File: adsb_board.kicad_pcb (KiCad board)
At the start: 2 copper layers, 50 x 25 mm, 13 parts, among them J1 Conn_Coaxial, J2 Conn_Coaxial, J3 USB_B_Micro, U1 TA1090EC, U2 TA1090EC, U3 PSA4-5043+

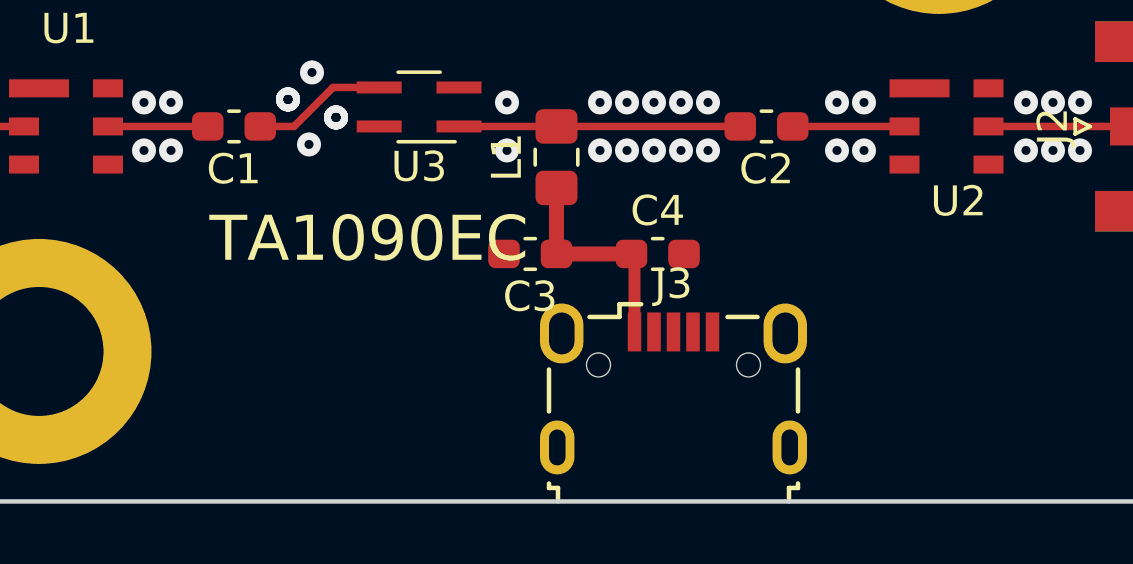
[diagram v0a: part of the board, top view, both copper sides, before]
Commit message: add ferrite bead in supply line
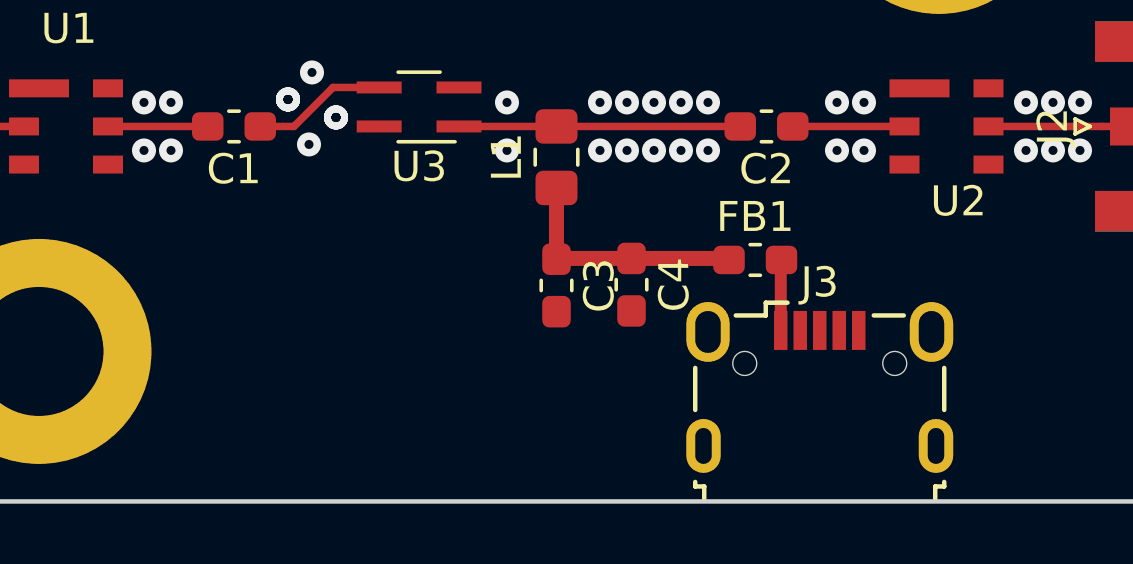
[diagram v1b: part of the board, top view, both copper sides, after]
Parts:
- added FB1: Ferrite_Bead, Resistor_SMD:R_0603_1608Metric_Pad1.05x0.95mm_HandSolder, F.Cu at (133.9, 92.0)
- moved J3 4.88 mm to (136.0, 96.2)
- moved C3 1.37 mm to (127.2, 92.8), turned to 270 degrees
- moved C4 1.35 mm to (129.8, 92.8), turned to 270 degrees
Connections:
- J3 pad 1: /VCC -> Net-(FB1-Pad2)
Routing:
- net Net-(FB1-Pad2): track 0.00 -> 2.36 mm
- net /VCC: track 7.34 -> 8.16 mm
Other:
- board text removed: "TA1090EC"
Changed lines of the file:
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@@
   (general
     (thickness 1.6)
-    (drawings 8)
-    (tracks 57)
+    (drawings 7)
+    (tracks 60)
     (zones 0)
-    (modules 13)
-    (nets 13)
+    (modules 14)
+    (nets 14)
   )
   (page A4)
@@
     (35 F.Paste user hide)
     (36 B.SilkS user hide)
-    (37 F.SilkS user hide)
+    (37 F.SilkS user)
     (38 B.Mask user hide)
     (39 F.Mask user hide)
-    (40 Dwgs.User user)
+    (40 Dwgs.User user hide)
     (41 Cmts.User user)
-    (42 Eco1.User user)
+    (42 Eco1.User user hide)
     (43 Eco2.User user)
     (44 Edge.Cuts user)
     (45 Margin user)
     (46 B.CrtYd user)
-    (47 F.CrtYd user)
+    (47 F.CrtYd user hide)
     (48 B.Fab user)
-    (49 F.Fab user)
+    (49 F.Fab user hide)
   )
   (setup
-    (last_trace_width 0.25)
+    (last_trace_width 0.5)
     (user_trace_width 0.3)
     (user_trace_width 0.4)
@@
   (net 11 "Net-(J3-Pad3)")
   (net 12 "Net-(J3-Pad4)")
+  (net 13 "Net-(FB1-Pad2)")
   (net_class Default "Dies ist die voreingestellte Netzklasse."
     (clearance 0.2)
@@
     (add_net "Net-(C2-Pad1)")
     (add_net "Net-(C2-Pad2)")
+    (add_net "Net-(FB1-Pad2)")
     (add_net "Net-(J3-Pad2)")
     (add_net "Net-(J3-Pad3)")
@@
     (add_net "Net-(U3-Pad4)")
   )
+  (module Resistor_SMD:R_0603_1608Metric_Pad1.05x0.95mm_HandSolder (layer F.Cu)
+    (at 133.875 91.95)
+    (descr "Resistor SMD 0603 (1608 Metric), square (rectangular) end terminal, IPC_7351 nominal with elongated pad for handsoldering. (Body size source: http://www.tortai-tech.com/upload/download/2011102023233369053.pdf), generated with kicad-footprint-generator")
+    (tags "resistor handsolder")
+    (attr smd)
+    (fp_text reference FB1 (at 0 -1.43) (layer F.SilkS)
+      (effects (font (size 1 1) (thickness 0.15)))
+    )
+    (fp_text value Ferrite_Bead (at 6.375 0.05) (layer F.Fab)
+      (effects (font (size 1 1) (thickness 0.15)))
+    )
+    (fp_line (start -0.8 0.4) (end -0.8 -0.4) (layer F.Fab) (width 0.1))
+    (fp_line (start -0.8 -0.4) (end 0.8 -0.4) (layer F.Fab) (width 0.1))
+    (fp_line (start 0.8 -0.4) (end 0.8 0.4) (layer F.Fab) (width 0.1))
+    (fp_line (start 0.8 0.4) (end -0.8 0.4) (layer F.Fab) (width 0.1))
+    (fp_line (start -0.171267 -0.51) (end 0.171267 -0.51) (layer F.SilkS) (width 0.12))
+    (fp_line (start -0.171267 0.51) (end 0.171267 0.51) (layer F.SilkS) (width 0.12))
+    (fp_line (start -1.65 0.73) (end -1.65 -0.73) (layer F.CrtYd) (width 0.05))
+    (fp_line (start -1.65 -0.73) (end 1.65 -0.73) (layer F.CrtYd) (width 0.05))
+    (fp_line (start 1.65 -0.73) (end 1.65 0.73) (layer F.CrtYd) (width 0.05))
+    (fp_line (start 1.65 0.73) (end -1.65 0.73) (layer F.CrtYd) (width 0.05))
+    (fp_text user %R (at 0 -0.95) (layer F.Fab)
+      (effects (font (size 0.4 0.4) (thickness 0.06)))
+    )
+    (pad 1 smd roundrect (at -0.875 0) (size 1.05 0.95) (layers F.Cu F.Paste F.Mask) (roundrect_rratio 0.25)
+      (net 4 /VCC))
+    (pad 2 smd roundrect (at 0.875 0) (size 1.05 0.95) (layers F.Cu F.Paste F.Mask) (roundrect_rratio 0.25)
+      (net 13 "Net-(FB1-Pad2)"))
+    (model ${KISYS3DMOD}/Resistor_SMD.3dshapes/R_0603_1608Metric.wrl
+      (at (xyz 0 0 0))
+      (scale (xyz 1 1 1))
+      (rotate (xyz 0 0 0))
+    )
+  )
   (module Connector_USB:USB_Micro-B_Wuerth_629105150521 (layer F.Cu)
-    (at 131.15 96.25)
+    (at 136.025 96.2)
     (descr "USB Micro-B receptacle, http://www.mouser.com/ds/2/445/629105150521-469306.pdf")
     (tags "usb micro receptacle")
@@
       (net 10 "Net-(J3-Pad2)"))
     (pad 1 smd rect (at -1.3 -1.9) (size 0.45 1.3) (layers F.Cu F.Paste F.Mask)
-      (net 4 /VCC))
+      (net 13 "Net-(FB1-Pad2)"))
     (model ${KISYS3DMOD}/Connector_USB.3dshapes/USB_Micro-B_Wuerth_629105150521.wrl
       (at (xyz 0 0 0))
@@
   )
   (module Capacitor_SMD:C_0603_1608Metric_Pad1.05x0.95mm_HandSolder (layer F.Cu)
-    (at 130.625 91.75)
+    (at 129.75 92.775 270)
     (descr "Capacitor SMD 0603 (1608 Metric), square (rectangular) end terminal, IPC_7351 nominal with elongated pad for handsoldering. (Body size source: http://www.tortai-tech.com/upload/download/2011102023233369053.pdf), generated with kicad-footprint-generator")
     (tags "capacitor handsolder")
     (attr smd)
-    (fp_text reference C4 (at 0 -1.43) (layer F.SilkS)
-      (effects (font (size 1 1) (thickness 0.15)))
-    )
-    (fp_text value 4.7uF (at 4.375 0) (layer F.Fab)
-      (effects (font (size 1 1) (thickness 0.15)))
-    )
-    (fp_text user %R (at 0 0) (layer F.Fab)
+    (fp_text reference C4 (at 0 -1.43 270) (layer F.SilkS)
+      (effects (font (size 1 1) (thickness 0.15)))
+    )
+    (fp_text value 4.7uF (at 3.925 0 270) (layer F.Fab)
+      (effects (font (size 1 1) (thickness 0.15)))
+    )
+    (fp_text user %R (at 0 1 270) (layer F.Fab)
       (effects (font (size 0.4 0.4) (thickness 0.06)))
     )
@@
     (fp_line (start -0.8 -0.4) (end 0.8 -0.4) (layer F.Fab) (width 0.1))
     (fp_line (start -0.8 0.4) (end -0.8 -0.4) (layer F.Fab) (width 0.1))
-    (pad 2 smd roundrect (at 0.875 0) (size 1.05 0.95) (layers F.Cu F.Paste F.Mask) (roundrect_rratio 0.25)
-      (net 1 /GND))
-    (pad 1 smd roundrect (at -0.875 0) (size 1.05 0.95) (layers F.Cu F.Paste F.Mask) (roundrect_rratio 0.25)
+    (pad 2 smd roundrect (at 0.875 0 270) (size 1.05 0.95) (layers F.Cu F.Paste F.Mask) (roundrect_rratio 0.25)
+      (net 1 /GND))
+    (pad 1 smd roundrect (at -0.875 0 270) (size 1.05 0.95) (layers F.Cu F.Paste F.Mask) (roundrect_rratio 0.25)
       (net 4 /VCC))
     (model ${KISYS3DMOD}/Capacitor_SMD.3dshapes/C_0603_1608Metric.wrl
@@
   )
   (module Capacitor_SMD:C_0603_1608Metric_Pad1.05x0.95mm_HandSolder (layer F.Cu)
-    (at 126.375 91.75 180)
+    (at 127.25 92.8 270)
     (descr "Capacitor SMD 0603 (1608 Metric), square (rectangular) end terminal, IPC_7351 nominal with elongated pad for handsoldering. (Body size source: http://www.tortai-tech.com/upload/download/2011102023233369053.pdf), generated with kicad-footprint-generator")
     (tags "capacitor handsolder")
     (attr smd)
-    (fp_text reference C3 (at 0 -1.43 180) (layer F.SilkS)
-      (effects (font (size 1 1) (thickness 0.15)))
-    )
-    (fp_text value 1000pF (at 4.875 0 180) (layer F.Fab)
-      (effects (font (size 1 1) (thickness 0.15)))
-    )
-    (fp_text user %R (at 0 0 180) (layer F.Fab)
+    (fp_text reference C3 (at 0 -1.43 270) (layer F.SilkS)
+      (effects (font (size 1 1) (thickness 0.15)))
+    )
+    (fp_text value 1000pF (at 2.7 1.8 270) (layer F.Fab)
+      (effects (font (size 1 1) (thickness 0.15)))
+    )
+    (fp_text user %R (at 0 1 270) (layer F.Fab)
       (effects (font (size 0.4 0.4) (thickness 0.06)))
     )
@@
     (fp_line (start -0.8 -0.4) (end 0.8 -0.4) (layer F.Fab) (width 0.1))
     (fp_line (start -0.8 0.4) (end -0.8 -0.4) (layer F.Fab) (width 0.1))
-    (pad 2 smd roundrect (at 0.875 0 180) (size 1.05 0.95) (layers F.Cu F.Paste F.Mask) (roundrect_rratio 0.25)
-      (net 1 /GND))
-    (pad 1 smd roundrect (at -0.875 0 180) (size 1.05 0.95) (layers F.Cu F.Paste F.Mask) (roundrect_rratio 0.25)
+    (pad 2 smd roundrect (at 0.875 0 270) (size 1.05 0.95) (layers F.Cu F.Paste F.Mask) (roundrect_rratio 0.25)
+      (net 1 /GND))
+    (pad 1 smd roundrect (at -0.875 0 270) (size 1.05 0.95) (layers F.Cu F.Paste F.Mask) (roundrect_rratio 0.25)
       (net 4 /VCC))
     (model ${KISYS3DMOD}/Capacitor_SMD.3dshapes/C_0603_1608Metric.wrl
@@
       (effects (font (size 1 1) (thickness 0.15)))
     )
-    (fp_text user %R (at 0 0 180) (layer F.Fab)
+    (fp_text user %R (at 0 -1 180) (layer F.Fab)
       (effects (font (size 0.4 0.4) (thickness 0.06)))
     )
@@
       (effects (font (size 1 1) (thickness 0.15)))
     )
-    (fp_text user %R (at 0 0 180) (layer F.Fab)
+    (fp_text user %R (at 0 -1 180) (layer F.Fab)
       (effects (font (size 0.4 0.4) (thickness 0.06)))
     )
@@
       (effects (font (size 1 1) (thickness 0.15)))
     )
-    (fp_text user %R (at 0 0 90) (layer F.Fab)
+    (fp_text user %R (at 0.025 -1.25 90) (layer F.Fab)
       (effects (font (size 0.5 0.5) (thickness 0.08)))
     )
@@
     (pad 1 thru_hole circle (at 0 0) (size 7.5 7.5) (drill 4.3) (layers *.Cu *.Mask)
       (net 1 /GND))
-  )
-  (gr_text TA1090EC (at 121 91.25) (layer F.SilkS)
-    (effects (font (size 1.5 1.5) (thickness 0.3)))
   )
   (gr_text OUTPUT (at 147.25 79.25 90) (layer F.SilkS)
@@
   (segment (start 145.45 87.5) (end 141.65 87.5) (width 0.25) (layer F.Cu) (net 3))
   (segment (start 147.5 87.5) (end 145.45 87.5) (width 0.25) (layer F.Cu) (net 3))
-  (segment (start 127.25 91.75) (end 127.25 89.55) (width 0.5) (layer F.Cu) (net 4))
-  (segment (start 129.75 91.75) (end 127.25 91.75) (width 0.5) (layer F.Cu) (net 4))
-  (segment (start 129.85 91.85) (end 129.75 91.75) (width 0.4) (layer F.Cu) (net 4))
-  (segment (start 129.85 94.35) (end 129.85 91.85) (width 0.4) (layer F.Cu) (net 4))
+  (segment (start 132.95 91.9) (end 133 91.95) (width 0.5) (layer F.Cu) (net 4))
+  (segment (start 129.75 91.9) (end 132.95 91.9) (width 0.5) (layer F.Cu) (net 4))
+  (segment (start 127.275 91.9) (end 127.25 91.925) (width 0.5) (layer F.Cu) (net 4))
+  (segment (start 129.75 91.9) (end 127.275 91.9) (width 0.5) (layer F.Cu) (net 4))
+  (segment (start 127.25 91.925) (end 127.25 89.55) (width 0.5) (layer F.Cu) (net 4))
   (segment (start 124 87.5) (end 127.25 87.5) (width 0.25) (layer F.Cu) (net 5))
   (segment (start 127.25 87.5) (end 133.375 87.5) (width 0.25) (layer F.Cu) (net 5))
@@
   (segment (start 119.8 86.2) (end 121.34 86.2) (width 0.25) (layer F.Cu) (net 8))
   (segment (start 118.5 87.5) (end 119.8 86.2) (width 0.25) (layer F.Cu) (net 8))
+  (segment (start 134.725 91.975) (end 134.75 91.95) (width 0.4) (layer F.Cu) (net 13))
+  (segment (start 134.725 94.3) (end 134.725 91.975) (width 0.4) (layer F.Cu) (net 13))
   (zone (net 1) (net_name /GND) (layer B.Cu) (hatch edge 0.508)
     (connect_pads (clearance 0.508))
